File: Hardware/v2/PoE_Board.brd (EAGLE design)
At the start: 84.6 x 72.1 mm, 93 parts, among them U1 EDISON_CONNECTOR_FULLMOUNTING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, U2 LAN9512-JZX, U3 MAX4995AAUT+, U4 EDISON_CONNECTOR_FULLHEADER

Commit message: Ready for final review
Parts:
- added D5: (no value), SparkFun-DiscreteSemi:SMA-DIODE
- moved C37 1.28 mm to (15.8, 11.4)
- moved R25 1.28 mm to (3.56, 33.4)
- moved C10 1.27 mm to (39.2, 54.0)
- moved R10 1.27 mm to (70.7, 29.3)
- moved R21 1.27 mm to (70.7, 51.6)
- moved USB 1.27 mm to (74.5, 61.0)
- moved AG9805MT 1.27 mm to (53.3, 16.6)
- moved C1 1.27 mm to (41.2, 40.2)
- moved C13 1.27 mm to (47.3, 53.6)
- moved C14 1.27 mm to (42.2, 41.2)
- moved C17 1.27 mm to (36.1, 38.7)
- moved C19 1.27 mm to (60.3, 46.0)
- moved C20 1.27 mm to (60.3, 43.8)
- moved C23 1.27 mm to (61.5, 38.5)
- moved C30 1.27 mm to (40.8, 16.6)
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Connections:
- net S$13 renamed S$3
- removed net N$16: R11.1
- new net VB1: B1.~@2, X1.R10
- net S$28: now also R11.1
- net USB_VBUS: now also D5.C
- net VBUS1: now also D5.A
- net VDD3IO: now also X1.L1, X1.L3
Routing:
- net S$28: track 0.00 -> 70.5 mm, vias 0 -> 1
- net N$16: track 70.5 -> 0.00 mm, vias 1 -> 0
- net USB_VBUS: track 144.6 -> 158.1 mm
- net VBUS1: track 13.2 -> 23.8 mm, vias 2 -> 3
- net VDD3IO: track 148.9 -> 144.0 mm
- net S$3: track 36.9 -> 35.4 mm
- net FB: track 11.2 -> 12.0 mm
- net N$4: track 23.6 -> 22.8 mm
- net S$14: track 45.4 -> 44.9 mm
- net GND: track 139.2 -> 139.5 mm, vias 94 -> 97
- added copper zone on layer 16, net GND
- removed copper zone on layer 1, net FB

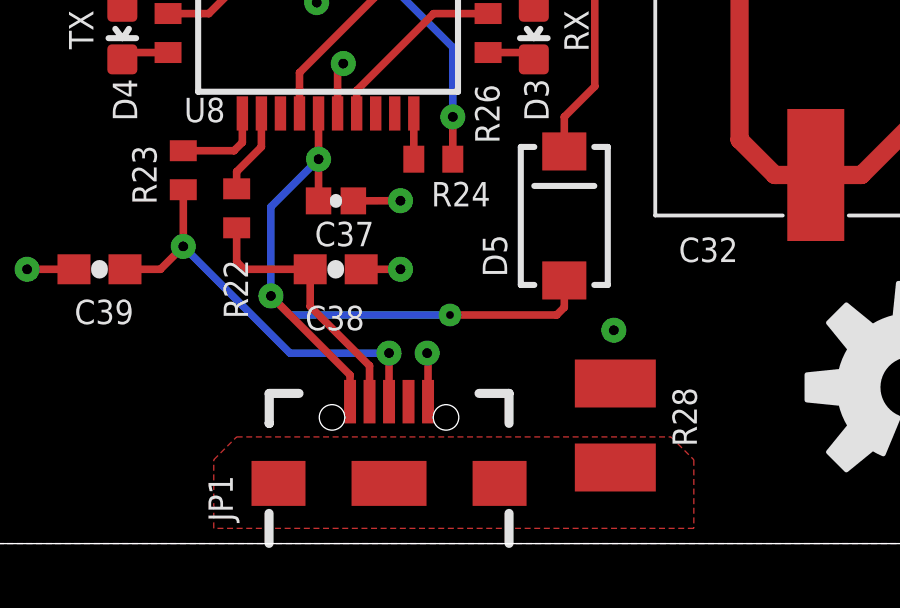
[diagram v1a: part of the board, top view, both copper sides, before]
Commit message: Made downstream USB traces the same length; minor changes to PoE board
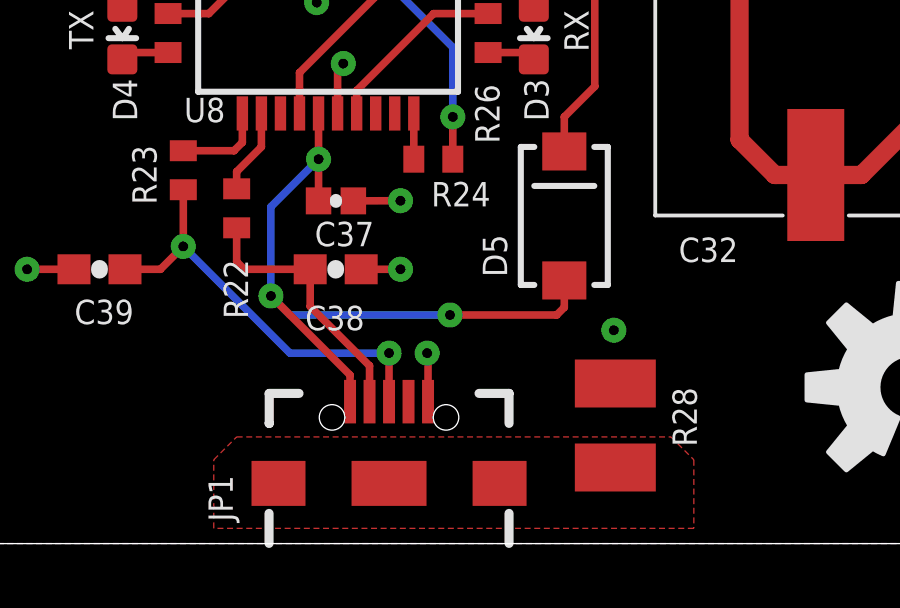
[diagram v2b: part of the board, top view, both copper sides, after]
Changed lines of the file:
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@@
 <wire x1="23.368" y1="7.874" x2="23.114" y2="7.62" width="0.254" layer="1"/>
 <wire x1="23.114" y1="7.62" x2="19.558" y2="7.62" width="0.254" layer="1"/>
-<via x="19.558" y="7.62" extent="1-16" drill="0.254"/>
+<via x="19.558" y="7.62" extent="1-16" drill="0.3302"/>
 <wire x1="19.558" y1="7.62" x2="14.224" y2="7.62" width="0.254" layer="16"/>
 <wire x1="14.224" y1="7.62" x2="13.589" y2="8.255" width="0.254" layer="16"/>

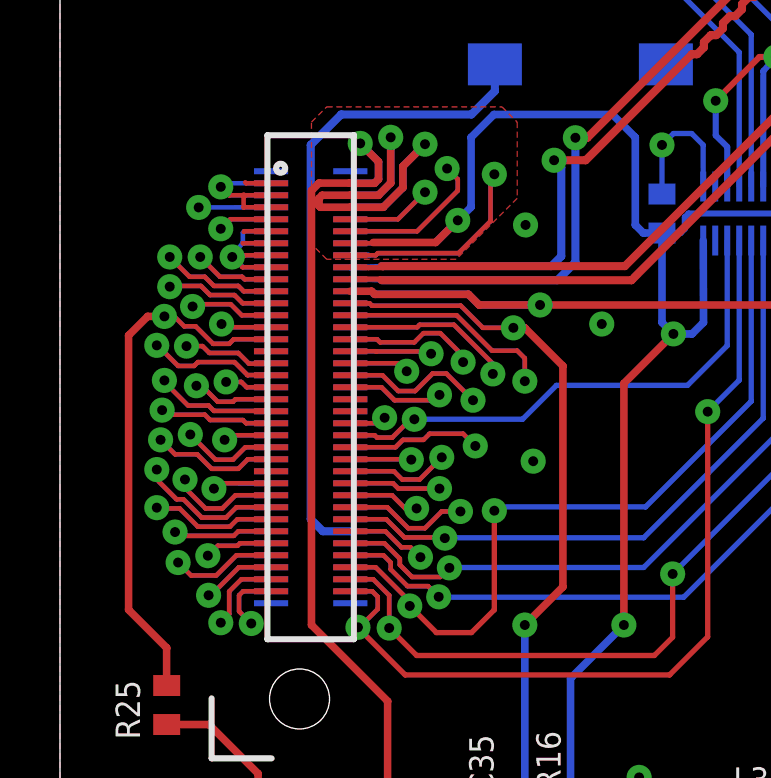
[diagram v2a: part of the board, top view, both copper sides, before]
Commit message: Fixed stub traces around Edison connector
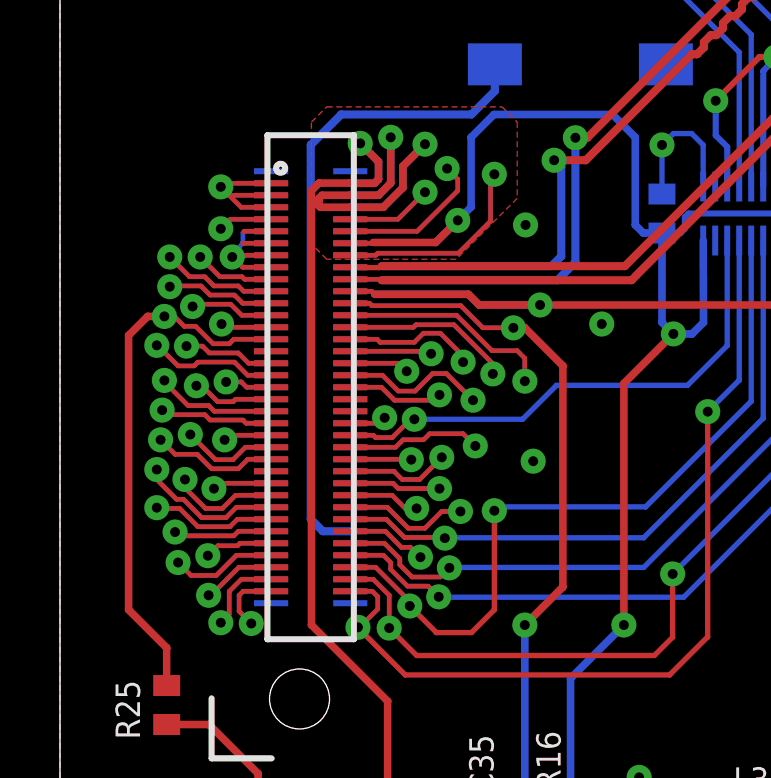
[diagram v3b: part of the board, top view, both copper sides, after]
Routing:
- net P55: track 10.9 -> 9.62 mm
- net GND: track 139.5 -> 140.5 mm, vias 97 -> 96
- net P51: track 4.87 -> 3.96 mm
- net P7: track 4.15 -> 3.62 mm

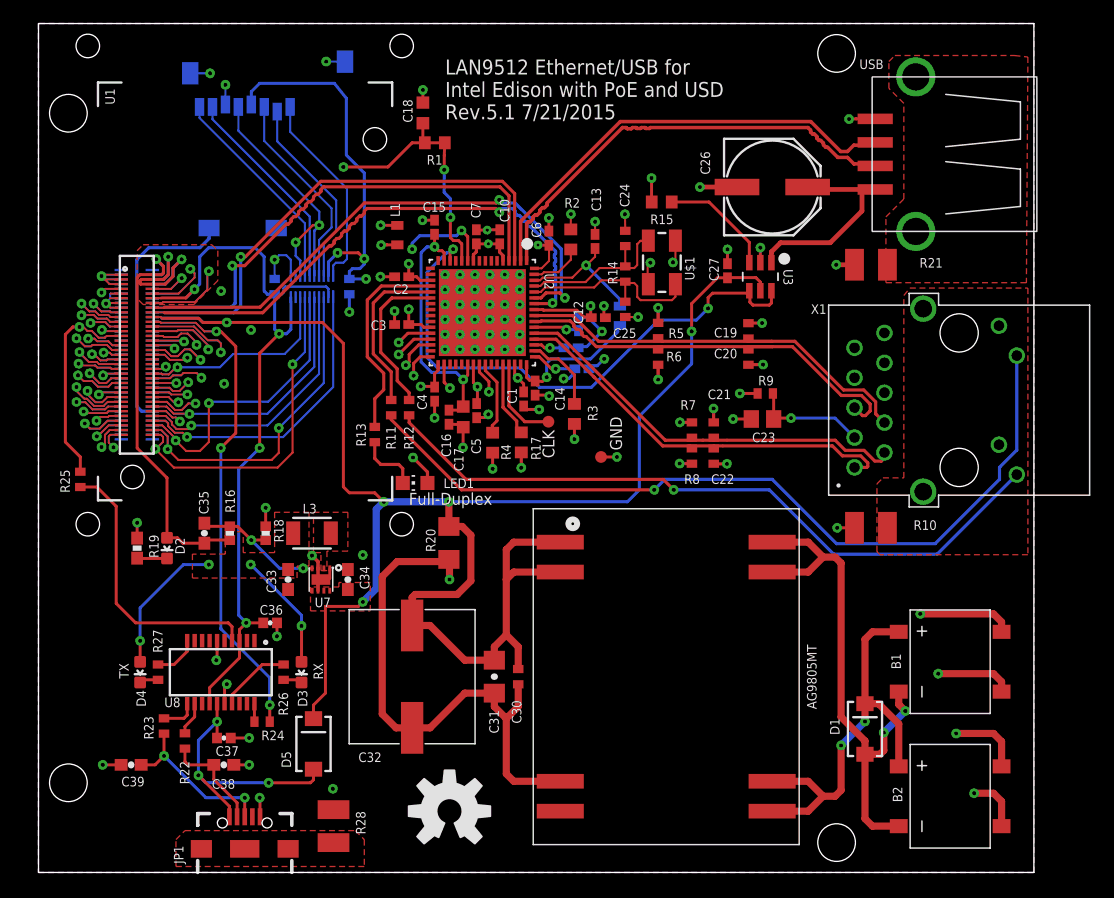
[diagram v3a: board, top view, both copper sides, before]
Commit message: Added LDO for power off VSYS, fixed SD card
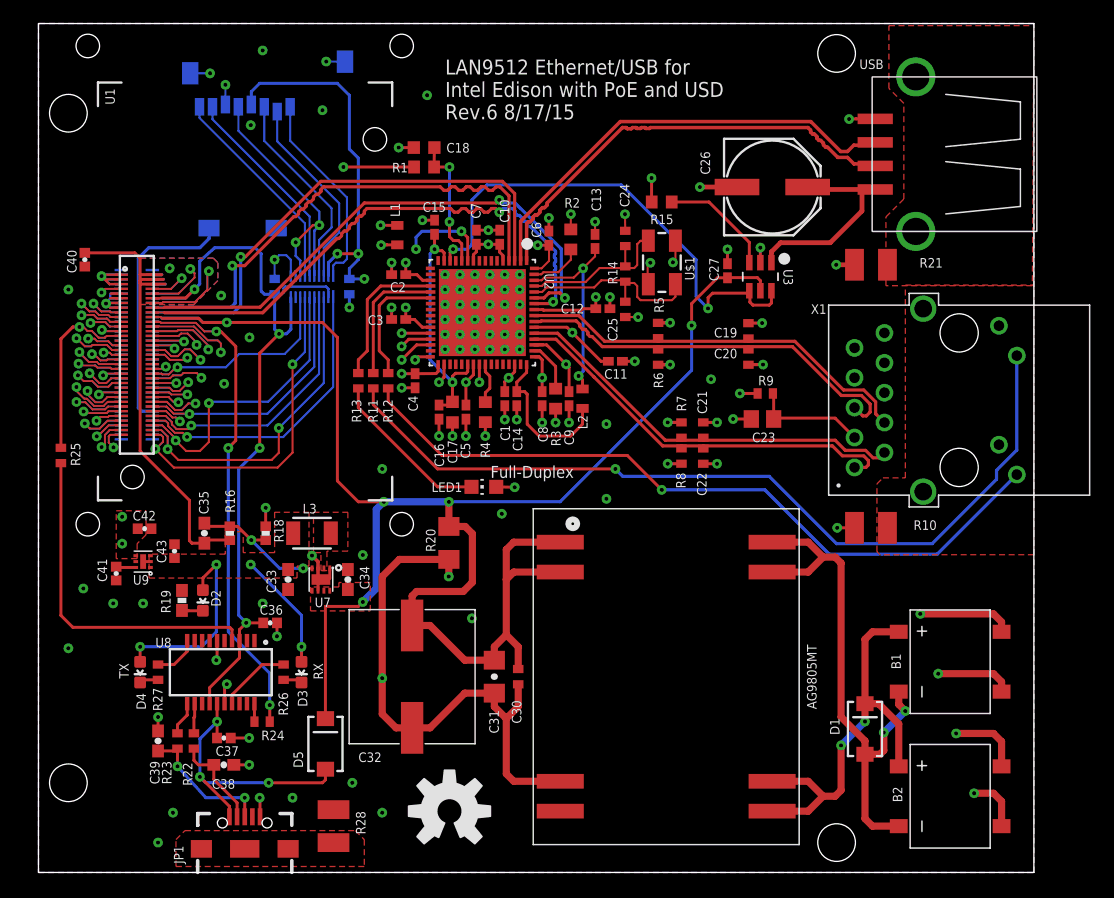
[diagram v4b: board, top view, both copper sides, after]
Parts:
- removed CLK_PAD: CLK, testpad:TP10R
- removed GNDPAD: GNDPAD, testpad:TP10R
- removed R17: 10K, resistor:R0603
- added C40, C41, C42, C43: (no value), SparkFun-Capacitors:0402-CAP
- added U9: (no value), PoEdev:6-UFDFN
- moved L2 7.72 mm to (46.2, 40.3), flipped to the top
- moved R19 5.85 mm to (12.2, 23.1)
- moved LED1 5.85 mm to (37.8, 32.8)
- moved D2 5.39 mm to (14.0, 23.1)
- moved R13 4.78 mm to (27.2, 41.8)
- moved C11 4.47 mm to (49.0, 43.4), flipped to the top, turned to 0 degrees
- moved C9 4.33 mm to (45.1, 40.3), flipped to the top, turned to 270 degrees
- moved C8 4.23 mm to (42.8, 40.3), flipped to the top, turned to 270 degrees
- moved C39 3.06 mm to (10.2, 11.2), turned to 90 degrees
- moved C18 2.95 mm to (32.8, 61.6), turned to 180 degrees
- moved R12 2.90 mm to (29.7, 41.8)
- moved R11 2.75 mm to (28.4, 41.8)
- moved R4 2.67 mm to (38.0, 39.1)
- moved R25 2.62 mm to (1.91, 35.4)
- moved R1 2.25 mm to (32.8, 59.9)
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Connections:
- removed net CLKOUT: CLK_PAD.TP, U2.45
- new net S$6: C41.1, U9.P6
- net GND: now also AG9805MT.P$3, C30.1, C31.1, C32.1, C40.1, C41.2, C42.2, C43.2, R20.1, U9.GND, U9.P2; no longer GNDPAD.TP, U6.19, USD.4
- net S$4: now also U1.10, U4.10; no longer R17.1, U2.44
- net S$5: now also U1.8, U4.8; no longer AG9805MT.P$3, C30.1, C31.1, C32.1, R20.1
- net VDD3IO: now also C42.1, U6.19, U9.P4, USD.4; no longer R17.2, U1.10, U1.8, U4.10, U4.8
- net VSYS: now also C40.2, C43.1, U9.P1, U9.P3
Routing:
- net S$5: track 44.6 -> 5.73 mm, vias 0 -> 1
- net N$19: track 5.34 -> 14.0 mm
- net CLKOUT: track 7.44 -> 0.00 mm
- net VDD3IO: track 144.0 -> 150.9 mm, vias 20 -> 21
- net N$1: track 11.5 -> 17.2 mm, vias 1 -> 2
- net N$23: track 47.8 -> 42.1 mm
- net GND: track 140.5 -> 145.9 mm, vias 96 -> 115
- net N$20: track 17.6 -> 12.4 mm
- net S$22: track 23.8 -> 28.9 mm
- net VDD33A: track 34.9 -> 40.0 mm, vias 13 -> 12
- net S$4: track 6.68 -> 10.1 mm, vias 0 -> 1
- net USB_VBUS: track 158.1 -> 154.8 mm
- net VSYS: track 86.7 -> 83.6 mm, vias 8 -> 6
- net N$17: track 59.7 -> 62.7 mm
- net N$15: track 14.1 -> 11.2 mm
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- added copper zone on layer 1, net VDD3IO
- added copper zone on layer 16, net VSYS
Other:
- board text added: "LAN9512 Ethernet/USB for Intel Edison with PoE and USD Rev.6 8/17/15"
- board text removed: "CLK"
- board text removed: "GND"
- board text removed: "LAN9512 Ethernet/USB for Intel Edison with PoE and USD Rev.5.1 7/21/2015"

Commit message: Changed R20
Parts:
- R20: device SparkFun-Resistors:1206 -> PoEdev:R1225
- moved R20 1.70 mm to (35.9, 26.7), turned to 0 degrees
- moved C13 1.07 mm to (46.2, 53.6)
- moved R2 0.45 mm to (44.8, 53.6)
- moved C6 0.31 mm to (43.4, 53.6)
- moved C12 0.13 mm to (48.0, 47.8)
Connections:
- net GND: now also R20.P$2; no longer R20.1
- net USB_VBUS: now also R20.P$1; no longer R20.2
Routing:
- net GND: track 145.9 -> 124.2 mm
- net USB_VBUS: track 154.8 -> 150.7 mm
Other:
- board text added: "LAN9512 Ethernet/USB for Intel Edison with PoE and USD Rev.6.1 8/17/15"
- board text removed: "LAN9512 Ethernet/USB for Intel Edison with PoE and USD Rev.6 8/17/15"

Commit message: Aesthetic changes for Ryan
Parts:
- moved C40 0.76 mm to (3.17, 52.1)
- moved C23 0.31 mm to (61.6, 38.2)
- moved D5 0.25 mm to (24.4, 11.2)
- moved C42 0.25 mm to (9.02, 29.5)
- moved R9 0.17 mm to (61.6, 40.6)
- moved C11 0.13 mm to (49.1, 43.4)
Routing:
- net N$23: track 42.1 -> 39.6 mm
- net VDD33A: track 40.0 -> 40.7 mm
- net VDD3IO: track 150.9 -> 151.6 mm
- net VSYS: track 83.6 -> 84.3 mm
- net USB_VBUS: track 150.7 -> 151.2 mm
- net GND: track 124.2 -> 124.0 mm, vias 115 -> 112
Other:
- board text added: "LAN9512 Ethernet/USB for Intel Edison with PoE and USD Rev.6.1 8/19/15"
- board text removed: "LAN9512 Ethernet/USB for Intel Edison with PoE and USD Rev.6.1 8/17/15"
